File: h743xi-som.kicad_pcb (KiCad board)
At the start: 2 copper layers, 3 parts, among them IC1 IS42S16160J-6BLI, IC2 S34ML01G200BHI000, U1 STM32H743XIH6

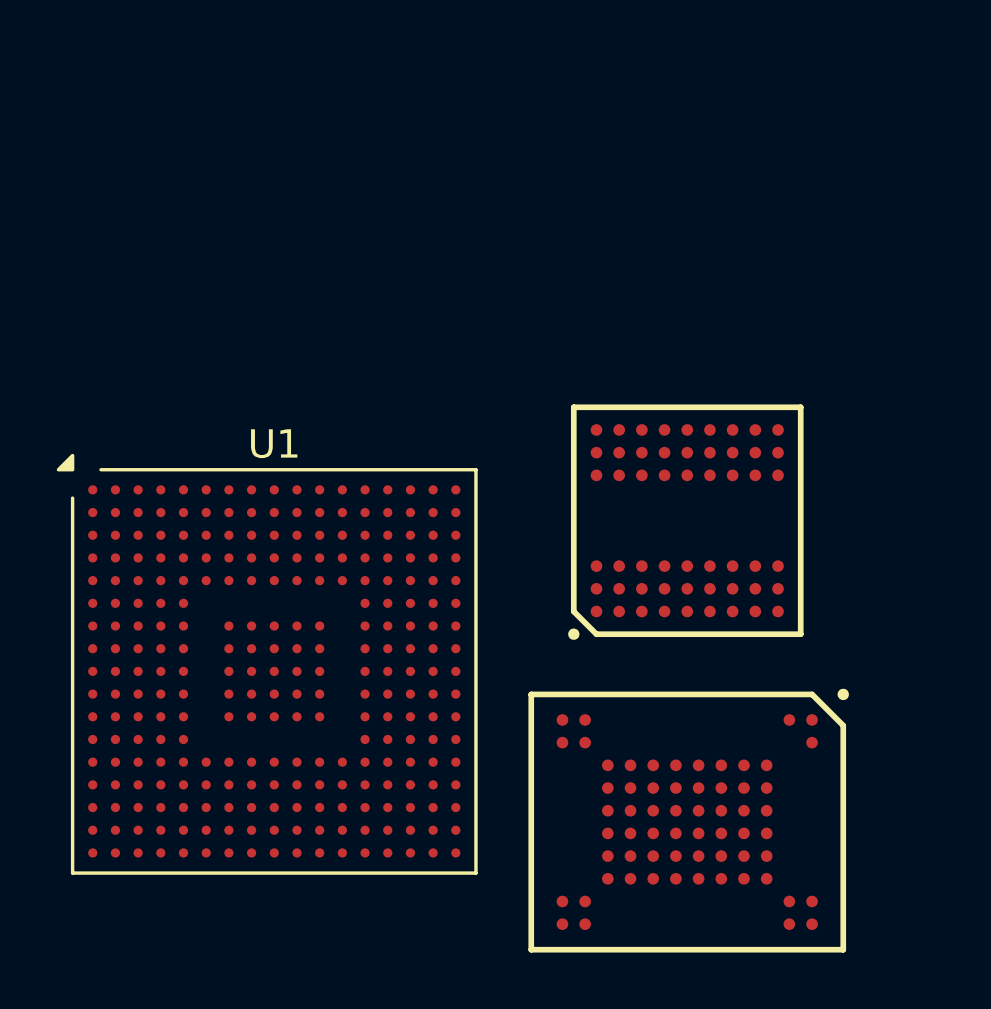
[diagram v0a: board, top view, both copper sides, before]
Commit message: Added my own memory libs, because snapeda or octopart gave me wrong pin library
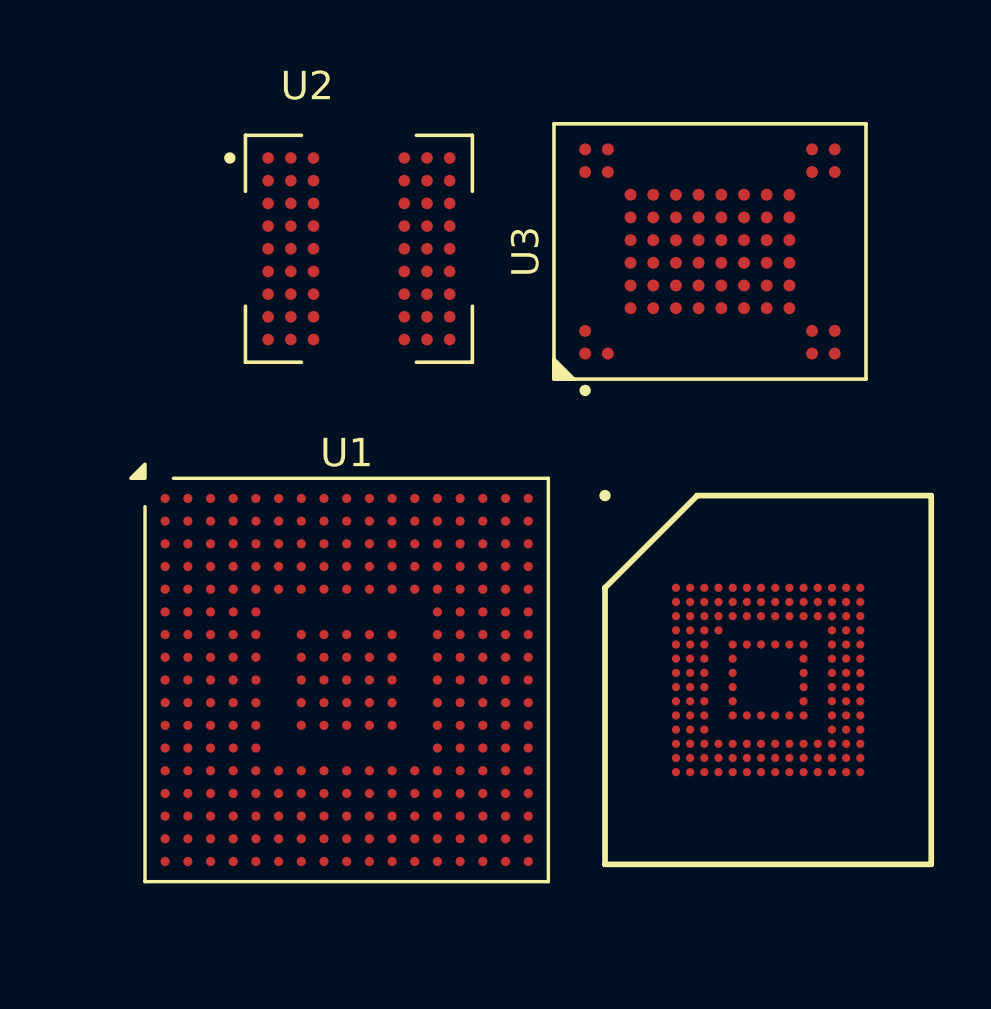
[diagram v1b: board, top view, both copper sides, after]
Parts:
- removed IC1: IS42S16160J-6BLI, IS42S16160J-6BLI:BGA54C80P9X9_800X800X120
- removed IC2: S34ML01G200BHI000, S34ML01G200BHI000:BGA63C80P10X12_900X1100X100
- added U2: IS42S16160J-6BLI, IS42S16160J-6BLI (1):BGA54C80P9X9_800X800X120, F.Cu at (143.4, 95.1)
- added U3: MX30LF1G18AC-XKI, lib:BGA63C80P10X12_900X1100X100N, F.Cu at (155.7, 95.2)
- added U4: KLM8G1GETF-B041, KLM8G1GETF-B0410:BGA153C50P14X14_1150X1300X80, F.Cu at (157.8, 110.3)
- moved U1 2.57 mm to (142.9, 110.3)
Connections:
- U1 pad A1: unconnected-(U1A-VSS-PadA1) -> GND
- U1 pad A17: unconnected-(U1A-VSS-PadA17) -> GND
- U1 pad A6: unconnected-(U1A-VDDLDO-PadA6) -> +3V3
- U1 pad A7: unconnected-(U1A-VCAP-PadA7) -> Net-(C29-Pad1)
- U1 pad B2: unconnected-(U1A-VSS-PadB2) -> GND
- U1 pad B6: unconnected-(U1A-VSS-PadB6) -> GND
- U1 pad C10: unconnected-(U1A-VSS-PadC10) -> GND
- U1 pad C13: unconnected-(U1A-VSS-PadC13) -> GND
- U1 pad C16: unconnected-(U1A-VSS-PadC16) -> GND
- U1 pad C17: unconnected-(U1A-VDDLDO-PadC17) -> +3V3
- U1 pad D17: unconnected-(U1A-VCAP-PadD17) -> Net-(C29-Pad1)
- U1 pad E11: unconnected-(U1A-VDD-PadE11) -> +3V3
- U1 pad E6: unconnected-(U1A-VDD-PadE6) -> +3V3
- U1 pad E9: unconnected-(U1A-VDD-PadE9) -> +3V3
- U1 pad F17: unconnected-(U1A-VDD33USB-PadF17) -> +3V3
- U1 pad F2: unconnected-(U1A-VSS-PadF2) -> GND
- U1 pad F5: unconnected-(U1A-VDD-PadF5) -> +3V3
- U1 pad G10: unconnected-(U1A-VSS-PadG10) -> GND
- U1 pad G11: unconnected-(U1A-VSS-PadG11) -> GND
- U1 pad G13: unconnected-(U1A-VDD-PadG13) -> +3V3
- U1 pad G16: unconnected-(U1A-VSS-PadG16) -> GND
- U1 pad G17: unconnected-(U1A-VDD50USB-PadG17) -> +3V3
- U1 pad G5: unconnected-(U1A-VDD-PadG5) -> +3V3
- U1 pad G7: unconnected-(U1A-VSS-PadG7) -> GND
- U1 pad G8: unconnected-(U1A-VSS-PadG8) -> GND
- U1 pad G9: unconnected-(U1A-VSS-PadG9) -> GND
- U1 pad H10: unconnected-(U1A-VSS-PadH10) -> GND
- U1 pad H11: unconnected-(U1A-VSS-PadH11) -> GND
- U1 pad H13: unconnected-(U1A-VDD-PadH13) -> +3V3
- U1 pad H5: unconnected-(U1A-VDD-PadH5) -> +3V3
- U1 pad H7: unconnected-(U1A-VSS-PadH7) -> GND
- U1 pad H8: unconnected-(U1A-VSS-PadH8) -> GND
- U1 pad H9: unconnected-(U1A-VSS-PadH9) -> GND
- U1 pad J10: unconnected-(U1A-VSS-PadJ10) -> GND
- U1 pad J11: unconnected-(U1A-VSS-PadJ11) -> GND
- U1 pad J13: unconnected-(U1A-VDD-PadJ13) -> +3V3
- U1 pad J16: unconnected-(U1A-VSS-PadJ16) -> GND
- U1 pad J17: unconnected-(U1A-VSS-PadJ17) -> GND
- U1 pad J3: unconnected-(U1A-VSS-PadJ3) -> GND
- U1 pad J7: unconnected-(U1A-VSS-PadJ7) -> GND
- U1 pad J8: unconnected-(U1A-VSS-PadJ8) -> GND
- U1 pad J9: unconnected-(U1A-VSS-PadJ9) -> GND
- U1 pad K10: unconnected-(U1A-VSS-PadK10) -> GND
- U1 pad K11: unconnected-(U1A-VSS-PadK11) -> GND
- U1 pad K13: unconnected-(U1A-VDD-PadK13) -> +3V3
- U1 pad K15: unconnected-(U1A-VSS-PadK15) -> GND
- U1 pad K5: unconnected-(U1A-VDD-PadK5) -> +3V3
- U1 pad K7: unconnected-(U1A-VSS-PadK7) -> GND
- U1 pad K8: unconnected-(U1A-VSS-PadK8) -> GND
- U1 pad K9: unconnected-(U1A-VSS-PadK9) -> GND
- U1 pad L1: unconnected-(U1C-VDDA-PadL1) -> +3V3
- U1 pad L10: unconnected-(U1C-VSS-PadL10) -> GND
- U1 pad L11: unconnected-(U1C-VSS-PadL11) -> GND
- U1 pad L13: unconnected-(U1C-VDD-PadL13) -> +3V3
- U1 pad L15: unconnected-(U1C-VSS-PadL15) -> GND
- U1 pad L5: unconnected-(U1C-VDD-PadL5) -> +3V3
- U1 pad L7: unconnected-(U1C-VSS-PadL7) -> GND
- U1 pad L8: unconnected-(U1C-VSS-PadL8) -> GND
- U1 pad L9: unconnected-(U1C-VSS-PadL9) -> GND
- U1 pad M13: unconnected-(U1C-VDD-PadM13) -> +3V3
- U1 pad M15: unconnected-(U1C-VSS-PadM15) -> GND
- U1 pad M5: unconnected-(U1C-VDD-PadM5) -> +3V3
- U1 pad N10: unconnected-(U1C-VDD-PadN10) -> +3V3
- U1 pad N11: unconnected-(U1C-VDD-PadN11) -> +3V3
- U1 pad N12: unconnected-(U1C-VDD-PadN12) -> +3V3
- U1 pad N16: unconnected-(U1C-VSS-PadN16) -> GND
- U1 pad N7: unconnected-(U1C-VDD-PadN7) -> +3V3
- U1 pad N8: unconnected-(U1C-VDD-PadN8) -> +3V3
- U1 pad P1: unconnected-(U1C-VSSA-PadP1) -> GND
- U1 pad P17: unconnected-(U1C-VDD-PadP17) -> +3V3
- U1 pad R4: unconnected-(U1C-VSS-PadR4) -> GND
- U1 pad R8: unconnected-(U1C-VSS-PadR8) -> GND
- U1 pad T12: unconnected-(U1C-VSS-PadT12) -> GND
- U1 pad U1: unconnected-(U1C-VSS-PadU1) -> GND
- U1 pad U11: unconnected-(U1C-VCAP-PadU11) -> Net-(U1C-VCAP)
- U1 pad U12: unconnected-(U1C-VDDLDO-PadU12) -> +3V3
- U1 pad U17: unconnected-(U1C-VSS-PadU17) -> GND

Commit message: Added octospi flash lib
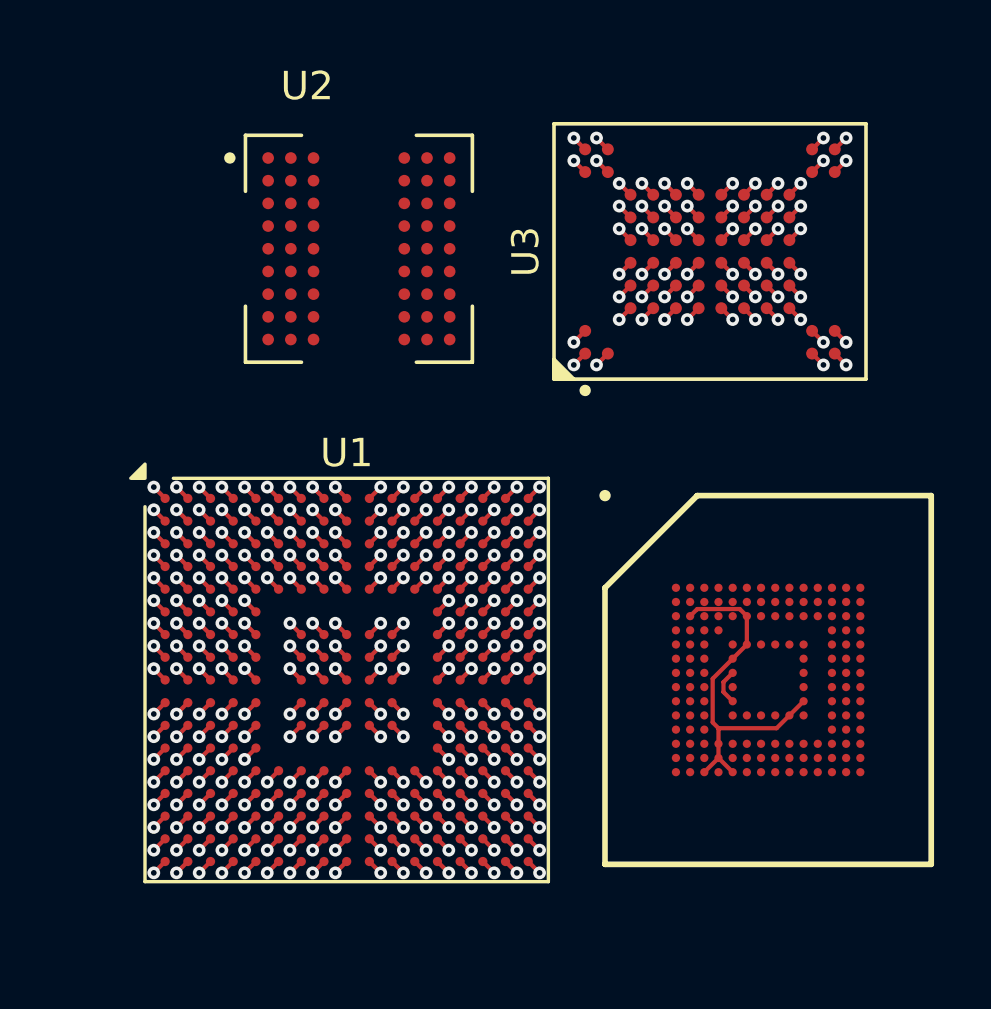
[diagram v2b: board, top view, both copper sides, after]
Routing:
- net +3V3: track 0.00 -> 30.1 mm, vias 0 -> 31
- net GND: track 0.00 -> 30.1 mm, vias 0 -> 51
- net Net-(C29-Pad1): track 0.00 -> 1.13 mm, vias 0 -> 2
- net unconnected-(U3-NC-PadM9): track 0.00 -> 0.57 mm, vias 0 -> 1
- net unconnected-(U3-NC-PadM2): track 0.00 -> 0.57 mm, vias 0 -> 1
- net unconnected-(U3-NC-PadM10): track 0.00 -> 0.57 mm, vias 0 -> 1
- net unconnected-(U3-NC-PadM1): track 0.00 -> 0.57 mm, vias 0 -> 1
- net unconnected-(U3-NC-PadL9): track 0.00 -> 0.57 mm, vias 0 -> 1
- net unconnected-(U3-NC-PadL2): track 0.00 -> 0.57 mm, vias 0 -> 1
- net unconnected-(U3-NC-PadL10): track 0.00 -> 0.57 mm, vias 0 -> 1
- net unconnected-(U3-NC-PadL1): track 0.00 -> 0.57 mm, vias 0 -> 1
- net unconnected-(U3-NC-PadJ3): track 0.00 -> 0.57 mm, vias 0 -> 1
- net unconnected-(U3-NC-PadG8): track 0.00 -> 0.57 mm, vias 0 -> 1
- net unconnected-(U3-NC-PadG3): track 0.00 -> 0.57 mm, vias 0 -> 1
- net unconnected-(U3-NC-PadE8): track 0.00 -> 0.57 mm, vias 0 -> 1
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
